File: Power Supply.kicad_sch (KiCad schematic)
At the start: 36 parts, among them IC1 LTM8074EY#PBF, IC2 LT3581IDE#PBF, IC3 LTM8074EY#PBF, IC4 LT3015IMSE-15#PBF, IC5 LT1963AES8-3.3#TRPBF, J5 Conn_01x02

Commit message: fatto piano di power
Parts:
- added NT1: NetTie_4, NetTie:NetTie-4_SMD_Pad0.5mm, symbol Device:NetTie_4
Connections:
- net GND: now also NT1.4; no longer C1.2, C2.2, D1.1 (K)
- new net GND_diode: D1.1 (K), NT1.1
- new net GND_in: C2.2, NT1.3
- new net GND_out: C1.2, NT1.2

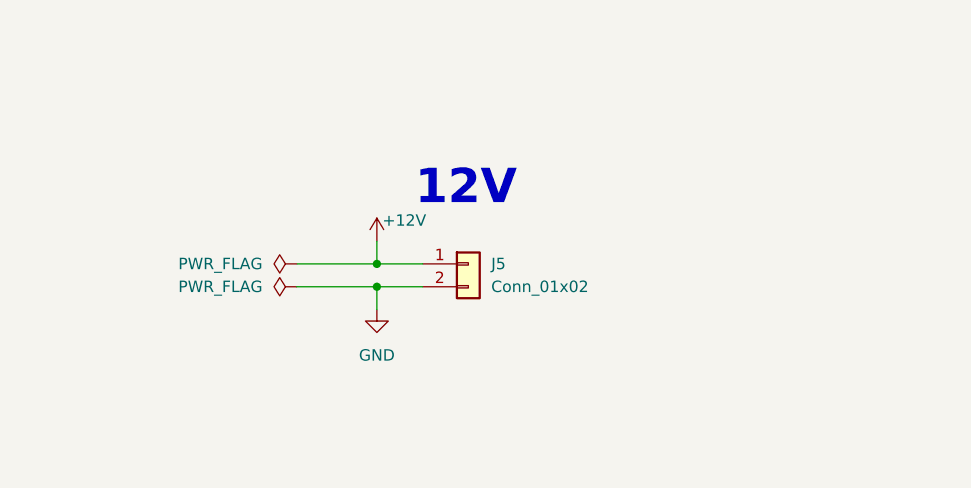
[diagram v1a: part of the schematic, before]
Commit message: modifiche per rispettare vincoli azienda
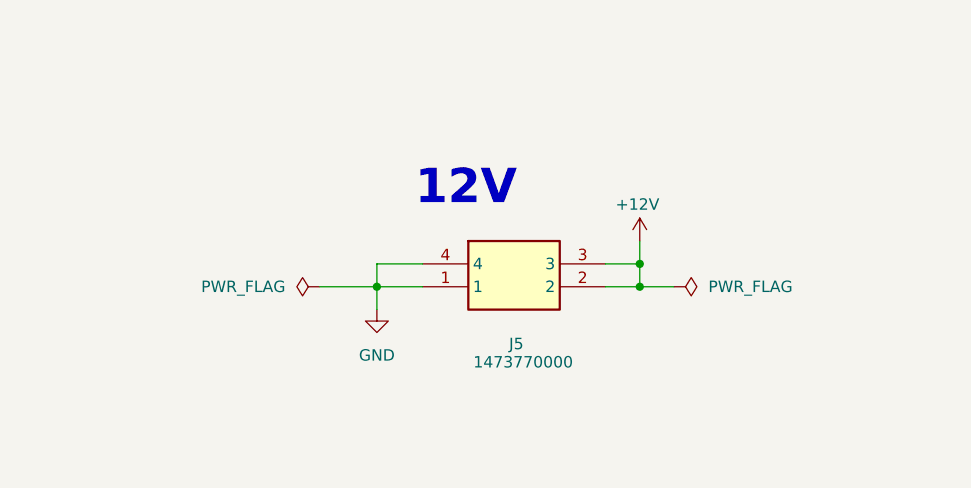
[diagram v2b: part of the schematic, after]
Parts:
- removed J5: Conn_01x02, SamacSys_Parts:1725656, symbol Connector_Generic:Conn_01x02
- added J5: 1473770000, SamacSys_Parts:1473770000, symbol SamacSys_Parts:1473770000
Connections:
- net +12V: now also J5.2, J5.3
- net GND: now also J5.1, J5.4

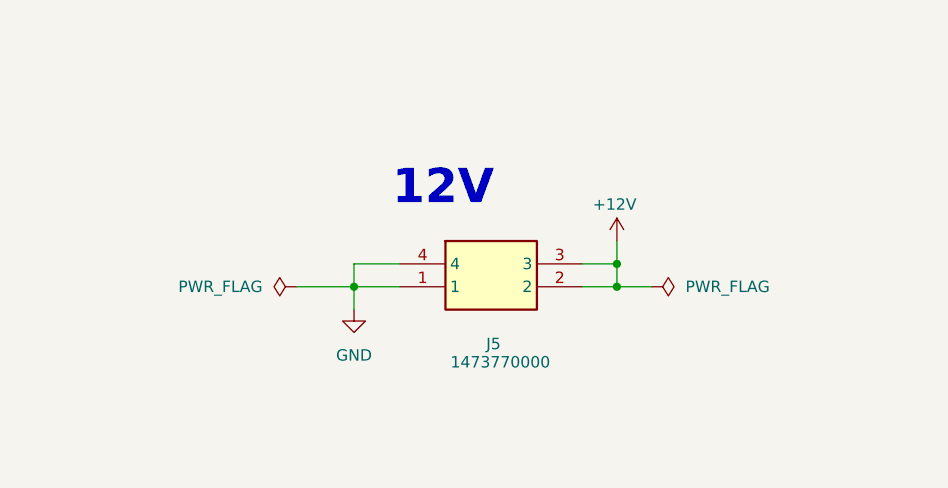
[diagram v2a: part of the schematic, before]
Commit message: terminato pcb e aggiunto script GUI
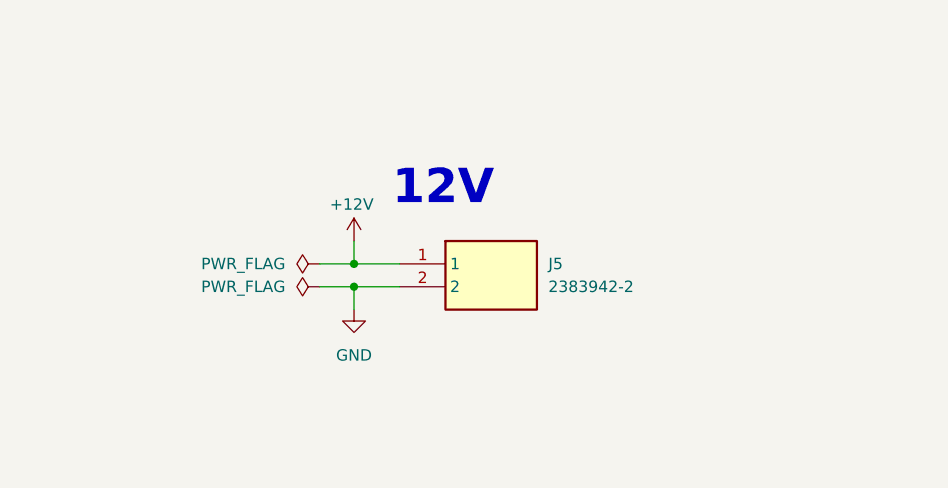
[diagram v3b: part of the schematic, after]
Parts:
- removed J5: 1473770000, SamacSys_Parts:1473770000, symbol SamacSys_Parts:1473770000
- added J5: 2383942-2, SamacSys_Parts:23839422, symbol SamacSys_Parts:2383942-2
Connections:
- net +12V: now also J5.1
- net GND: now also J5.2

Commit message: modificato pad esposti
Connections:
- net -5V: now also IC4.13 (EP)
- net GND: no longer IC4.13 (EP)
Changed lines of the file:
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@@
 	)
 	(junction
-		(at 278.13 123.19)
+		(at 275.59 123.19)
 		(diameter 0)
 		(color 0 0 0 0)
@@
 	)
 	(junction
+		(at 275.59 120.65)
+		(diameter 0)
+		(color 0 0 0 0)
+	)
+	(junction
+		(at 275.59 118.11)
+		(diameter 0)
+		(color 0 0 0 0)
+	)
+	(junction
 		(at 60.96 27.94)
 		(diameter 0)
@@
 	)
 	(junction
+		(at 292.1 146.05)
+		(diameter 0)
+		(color 0 0 0 0)
+	)
+	(junction
 		(at 71.12 43.18)
 		(diameter 0)
@@
 	)
 	(junction
+		(at 275.59 125.73)
+		(diameter 0)
+		(color 0 0 0 0)
+	)
+	(junction
 		(at 311.15 194.31)
 		(diameter 0)
@@
 	)
 	(junction
-		(at 278.13 120.65)
-		(diameter 0)
-		(color 0 0 0 0)
-	)
-	(junction
-		(at 278.13 118.11)
-		(diameter 0)
-		(color 0 0 0 0)
-	)
-	(junction
 		(at 325.12 129.54)
 		(diameter 0)
@@
 	)
 	(junction
-		(at 293.37 146.05)
-		(diameter 0)
-		(color 0 0 0 0)
-	)
-	(junction
 		(at 322.58 48.26)
 		(diameter 0)
@@
 	(wire
 		(pts
-			(xy 271.78 118.11) (xy 278.13 118.11)
+			(xy 271.78 118.11) (xy 275.59 118.11)
 		)
 		(stroke
@@
 	(wire
 		(pts
-			(xy 293.37 146.05) (xy 293.37 147.32)
-		)
-		(stroke
-			(width 0)
-			(type default)
-		)
-	)
-	(wire
-		(pts
 			(xy 97.79 90.17) (xy 96.52 90.17)
 		)
@@
 	(wire
 		(pts
-			(xy 278.13 146.05) (xy 293.37 146.05)
+			(xy 107.95 35.56) (xy 107.95 38.1)
 		)
 		(stroke
@@
 	(wire
 		(pts
-			(xy 107.95 35.56) (xy 107.95 38.1)
+			(xy 327.66 207.01) (xy 327.66 227.33)
 		)
 		(stroke
@@
 	(wire
 		(pts
-			(xy 327.66 207.01) (xy 327.66 227.33)
+			(xy 311.15 194.31) (xy 311.15 199.39)
 		)
 		(stroke
@@
 	(wire
 		(pts
-			(xy 311.15 194.31) (xy 311.15 199.39)
+			(xy 274.32 227.33) (xy 292.1 227.33)
 		)
 		(stroke
@@
 	(wire
 		(pts
-			(xy 274.32 227.33) (xy 292.1 227.33)
+			(xy 71.12 55.88) (xy 72.39 55.88)
 		)
 		(stroke
@@
 	(wire
 		(pts
-			(xy 71.12 55.88) (xy 72.39 55.88)
+			(xy 72.39 30.48) (xy 67.31 30.48)
 		)
 		(stroke
@@
 	(wire
 		(pts
-			(xy 72.39 30.48) (xy 67.31 30.48)
+			(xy 275.59 123.19) (xy 278.13 123.19)
 		)
 		(stroke
@@
 	(wire
 		(pts
+			(xy 275.59 118.11) (xy 278.13 118.11)
+		)
+		(stroke
+			(width 0)
+			(type default)
+		)
+	)
+	(wire
+		(pts
 			(xy 322.58 72.39) (xy 332.74 72.39)
 		)
@@
 	(wire
 		(pts
+			(xy 275.59 143.51) (xy 275.59 125.73)
+		)
+		(stroke
+			(width 0)
+			(type default)
+		)
+	)
+	(wire
+		(pts
 			(xy 313.69 45.72) (xy 313.69 60.96)
 		)
@@
 	(wire
 		(pts
-			(xy 293.37 146.05) (xy 308.61 146.05)
+			(xy 275.59 120.65) (xy 278.13 120.65)
+		)
+		(stroke
+			(width 0)
+			(type default)
+		)
+	)
+	(wire
+		(pts
+			(xy 278.13 146.05) (xy 292.1 146.05)
 		)
 		(stroke
@@
 	(wire
 		(pts
-			(xy 278.13 120.65) (xy 278.13 123.19)
+			(xy 275.59 120.65) (xy 275.59 123.19)
 		)
 		(stroke
@@
 	(wire
 		(pts
+			(xy 275.59 125.73) (xy 278.13 125.73)
+		)
+		(stroke
+			(width 0)
+			(type default)
+		)
+	)
+	(wire
+		(pts
 			(xy 119.38 30.48) (xy 119.38 31.75)
 		)
@@
 	(wire
 		(pts
-			(xy 278.13 123.19) (xy 278.13 125.73)
+			(xy 275.59 123.19) (xy 275.59 125.73)
 		)
 		(stroke
@@
 	(wire
 		(pts
-			(xy 45.72 133.35) (xy 57.15 133.35)
+			(xy 293.37 143.51) (xy 275.59 143.51)
 		)
 		(stroke
@@
 	(wire
 		(pts
-			(xy 105.41 43.18) (xy 113.03 43.18)
+			(xy 45.72 133.35) (xy 57.15 133.35)
 		)
 		(stroke
@@
 	(wire
 		(pts
-			(xy 265.43 217.17) (xy 275.59 217.17)
+			(xy 105.41 43.18) (xy 113.03 43.18)
 		)
 		(stroke
@@
 	(wire
 		(pts
-			(xy 293.37 143.51) (xy 293.37 146.05)
+			(xy 265.43 217.17) (xy 275.59 217.17)
 		)
 		(stroke
@@
 	(wire
 		(pts
+			(xy 292.1 146.05) (xy 308.61 146.05)
+		)
+		(stroke
+			(width 0)
+			(type default)
+		)
+	)
+	(wire
+		(pts
 			(xy 351.79 212.09) (xy 349.25 212.09)
 		)
@@
 	(wire
 		(pts
-			(xy 278.13 118.11) (xy 278.13 120.65)
+			(xy 275.59 118.11) (xy 275.59 120.65)
 		)
 		(stroke
@@
 	)
 	(symbol
-		(lib_id "power:GND")
-		(at 293.37 147.32 0)
-		(unit 1)
-		(exclude_from_sim no)
-		(in_bom yes)
-		(on_board yes)
-		(dnp no)
-		(property "Reference" "#PWR021"
-			(at 293.37 153.67 0)
-			(effects
-				(font
-					(size 1.27 1.27)
-				)
-				(hide yes)
-			)
-		)
-		(property "Value" "GND"
-			(at 293.37 151.13 0)
-			(effects
-				(font
-					(size 1.27 1.27)
-				)
-			)
-		)
-		(property "Footprint" ""
-			(at 293.37 147.32 0)
-			(effects
-				(font
-					(size 1.27 1.27)
-				)
-				(hide yes)
-			)
-		)
-		(property "Datasheet" ""
-			(at 293.37 147.32 0)
-			(effects
-				(font
-					(size 1.27 1.27)
-				)
-				(hide yes)
-			)
-		)
-		(property "Description" "Power symbol creates a global label with name \"GND\" , ground"
-			(at 293.37 147.32 0)
-			(effects
-				(font
-					(size 1.27 1.27)
-				)
-				(hide yes)
-			)
-		)
-		(pin "1"
-		)
-		(instances
-			(project "Schematico Basso Livello Tesi"
-				(path "/59e0b50f-8080-4ed9-9b83-2233f3b14569/c4428dd2-c041-417d-a9b2-0a34b803d32b"
-					(reference "#PWR021")
-					(unit 1)
-				)
-			)
-		)
-	)
-	(symbol
 		(lib_id "Device:R")
 		(at 140.97 156.21 90)
@@
 					(unit 1)
 				)
+			)
+		)
+	)
+	(symbol
+		(lib_id "power:GND")
+		(at 292.1 146.05 0)
+		(unit 1)
+		(exclude_from_sim no)
+		(in_bom yes)
+		(on_board yes)
+		(dnp no)
+		(fields_autoplaced yes)
+		(property "Reference" "#PWR021"
+			(at 292.1 152.4 0)
+			(effects
+				(font
+					(size 1.27 1.27)
+				)
+				(hide yes)
+			)
+		)
+		(property "Value" "GND"
+			(at 292.1 151.13 0)
+			(effects
+				(font
+					(size 1.27 1.27)
+				)
+			)
+		)
+		(property "Footprint" ""
+			(at 292.1 146.05 0)
+			(effects
+				(font
+					(size 1.27 1.27)
+				)
+				(hide yes)
+			)
+		)
+		(property "Datasheet" ""
+			(at 292.1 146.05 0)
+			(effects
+				(font
+					(size 1.27 1.27)
+				)
+				(hide yes)
+			)
+		)
+		(property "Description" "Power symbol creates a global label with name \"GND\" , ground"
+			(at 292.1 146.05 0)
+			(effects
+				(font
+					(size 1.27 1.27)
+				)
+				(hide yes)
+			)
+		)
+		(pin "1"
+		)
+		(instances
+			(project "A5256"
+				(path "/59e0b50f-8080-4ed9-9b83-2233f3b14569/c4428dd2-c041-417d-a9b2-0a34b803d32b"
+					(reference "#PWR021")
+					(unit 1)
+				)
